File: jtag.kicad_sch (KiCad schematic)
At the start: 5 parts, among them U1 LFE5U-12F-6BG256C

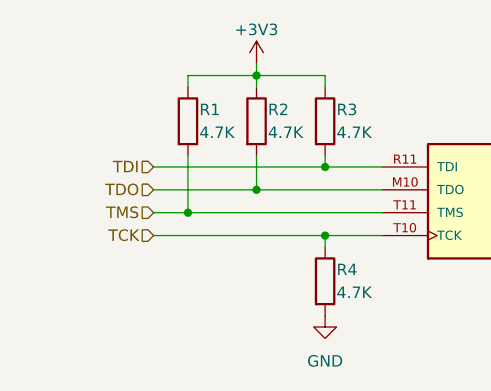
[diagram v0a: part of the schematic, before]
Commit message: Small routing tweaks, add breakout to schematic
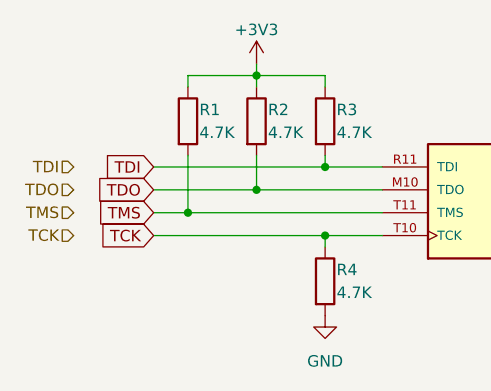
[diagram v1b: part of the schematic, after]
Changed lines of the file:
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@@
     (stroke (width 0) (type default))
   )
-  (hierarchical_label "TMS" (shape input) (at 115.57 44.45 180) (fields_autoplaced)
+  (global_label "TCK" (shape input) (at 115.57 46.99 180) (fields_autoplaced)
+    (effects (font (size 1.27 1.27)) (justify right))
+    (property "Intersheetrefs" "${INTERSHEET_REFS}" (at 109.1566 46.99 0)
+      (effects (font (size 1.27 1.27)) (justify right) hide)
+    )
+  )
+  (global_label "TDO" (shape input) (at 115.57 41.91 180) (fields_autoplaced)
+    (effects (font (size 1.27 1.27)) (justify right))
+    (property "Intersheetrefs" "${INTERSHEET_REFS}" (at 109.0961 41.91 0)
+      (effects (font (size 1.27 1.27)) (justify right) hide)
+    )
+  )
+  (global_label "TMS" (shape input) (at 115.57 44.45 180) (fields_autoplaced)
+    (effects (font (size 1.27 1.27)) (justify right))
+    (property "Intersheetrefs" "${INTERSHEET_REFS}" (at 109.0357 44.45 0)
+      (effects (font (size 1.27 1.27)) (justify right) hide)
+    )
+  )
+  (global_label "TDI" (shape input) (at 115.57 39.37 180) (fields_autoplaced)
+    (effects (font (size 1.27 1.27)) (justify right))
+    (property "Intersheetrefs" "${INTERSHEET_REFS}" (at 109.8218 39.37 0)
+      (effects (font (size 1.27 1.27)) (justify right) hide)
+    )
+  )
+  (hierarchical_label "TDI" (shape input) (at 106.68 39.37 180) (fields_autoplaced)
     (effects (font (size 1.27 1.27)) (justify right))
   )
-  (hierarchical_label "TDO" (shape input) (at 115.57 41.91 180) (fields_autoplaced)
+  (hierarchical_label "TMS" (shape input) (at 106.68 44.45 180) (fields_autoplaced)
     (effects (font (size 1.27 1.27)) (justify right))
   )
-  (hierarchical_label "TDI" (shape input) (at 115.57 39.37 180) (fields_autoplaced)
+  (hierarchical_label "TCK" (shape input) (at 106.68 46.99 180) (fields_autoplaced)
     (effects (font (size 1.27 1.27)) (justify right))
   )
-  (hierarchical_label "TCK" (shape input) (at 115.57 46.99 180) (fields_autoplaced)
+  (hierarchical_label "TDO" (shape input) (at 106.68 41.91 180) (fields_autoplaced)
     (effects (font (size 1.27 1.27)) (justify right))
   )

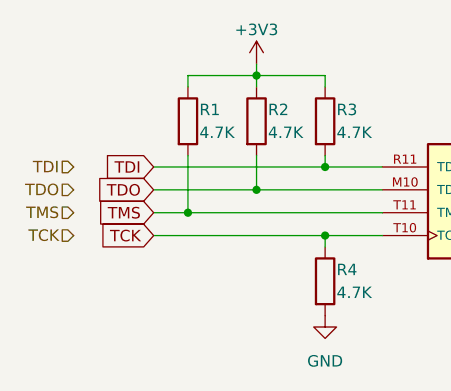
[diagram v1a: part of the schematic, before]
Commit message: Route flash + jtag resistors
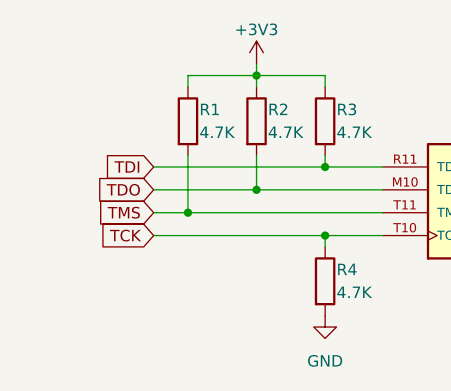
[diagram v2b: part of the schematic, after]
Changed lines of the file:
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@@
     )
-  )
-  (hierarchical_label "TDI" (shape input) (at 106.68 39.37 180) (fields_autoplaced)
-    (effects (font (size 1.27 1.27)) (justify right))
-  )
-  (hierarchical_label "TMS" (shape input) (at 106.68 44.45 180) (fields_autoplaced)
-    (effects (font (size 1.27 1.27)) (justify right))
-  )
-  (hierarchical_label "TCK" (shape input) (at 106.68 46.99 180) (fields_autoplaced)
-    (effects (font (size 1.27 1.27)) (justify right))
-  )
-  (hierarchical_label "TDO" (shape input) (at 106.68 41.91 180) (fields_autoplaced)
-    (effects (font (size 1.27 1.27)) (justify right))
   )
   (symbol (lib_id "Device:R") (at 127 34.29 0) (unit 1)

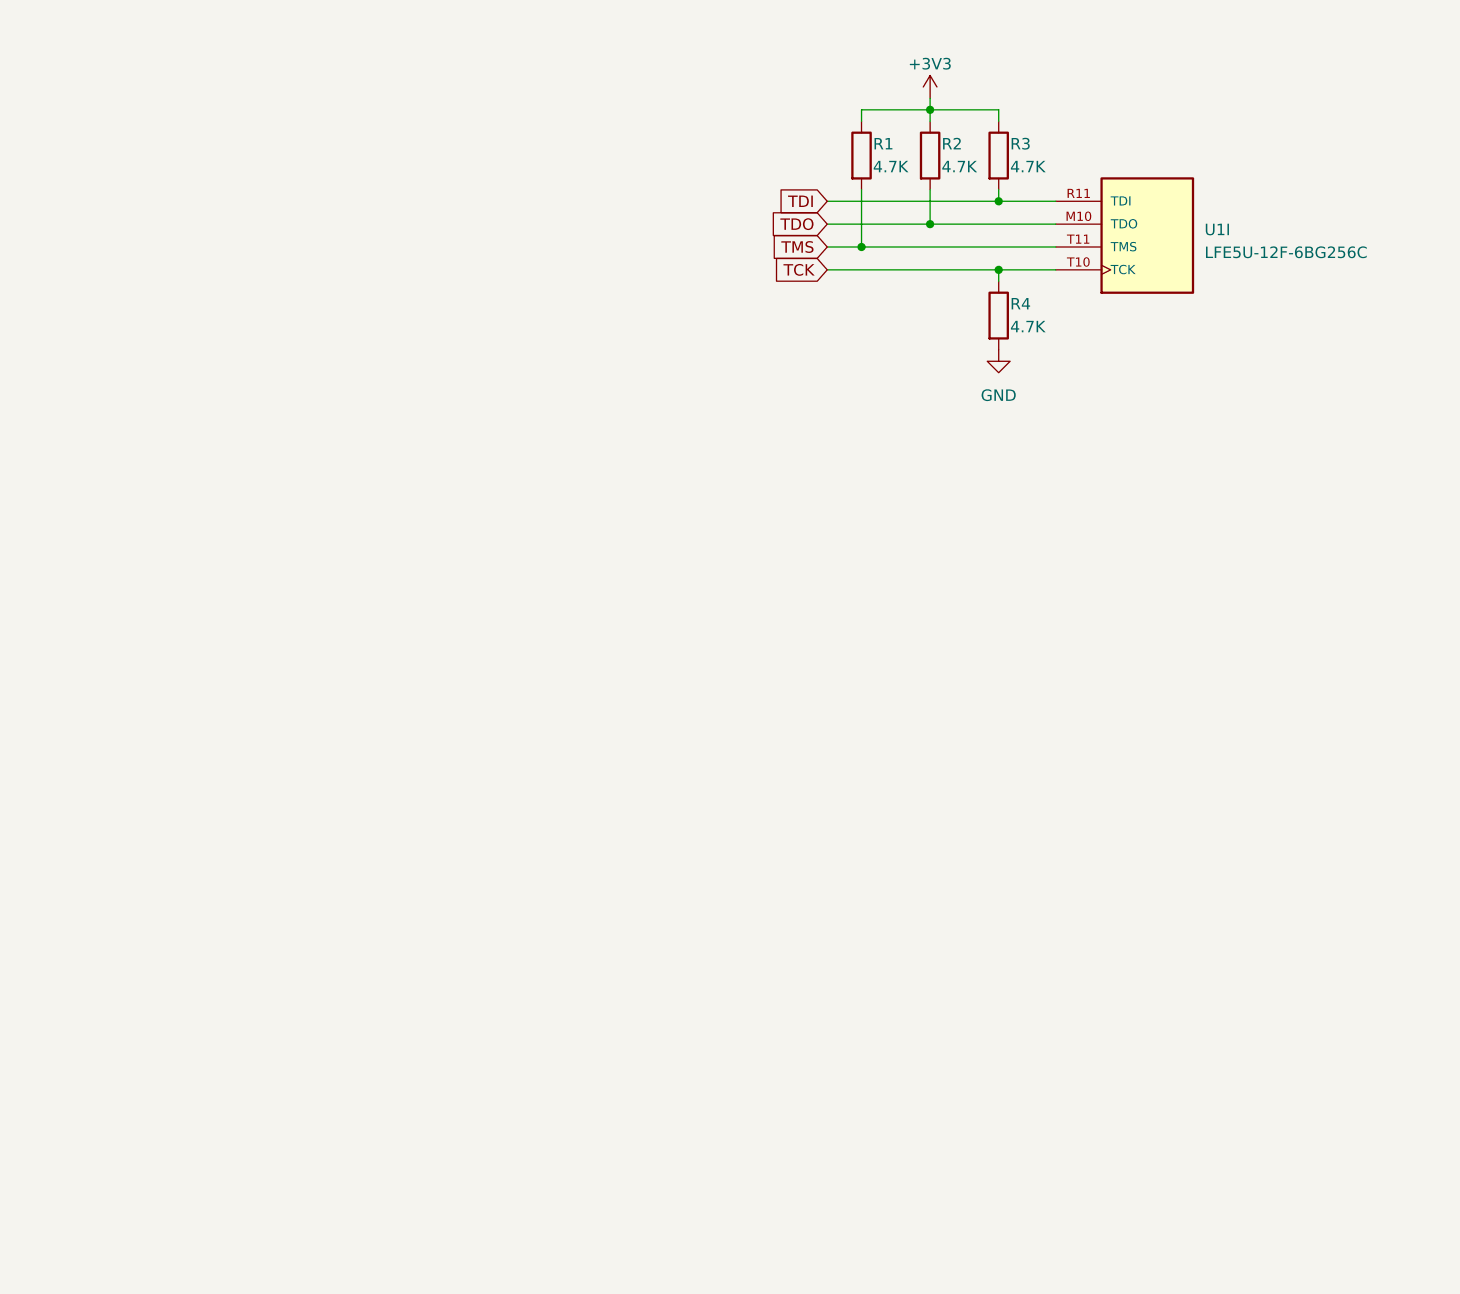
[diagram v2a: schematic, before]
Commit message: Route power, FTDI chip
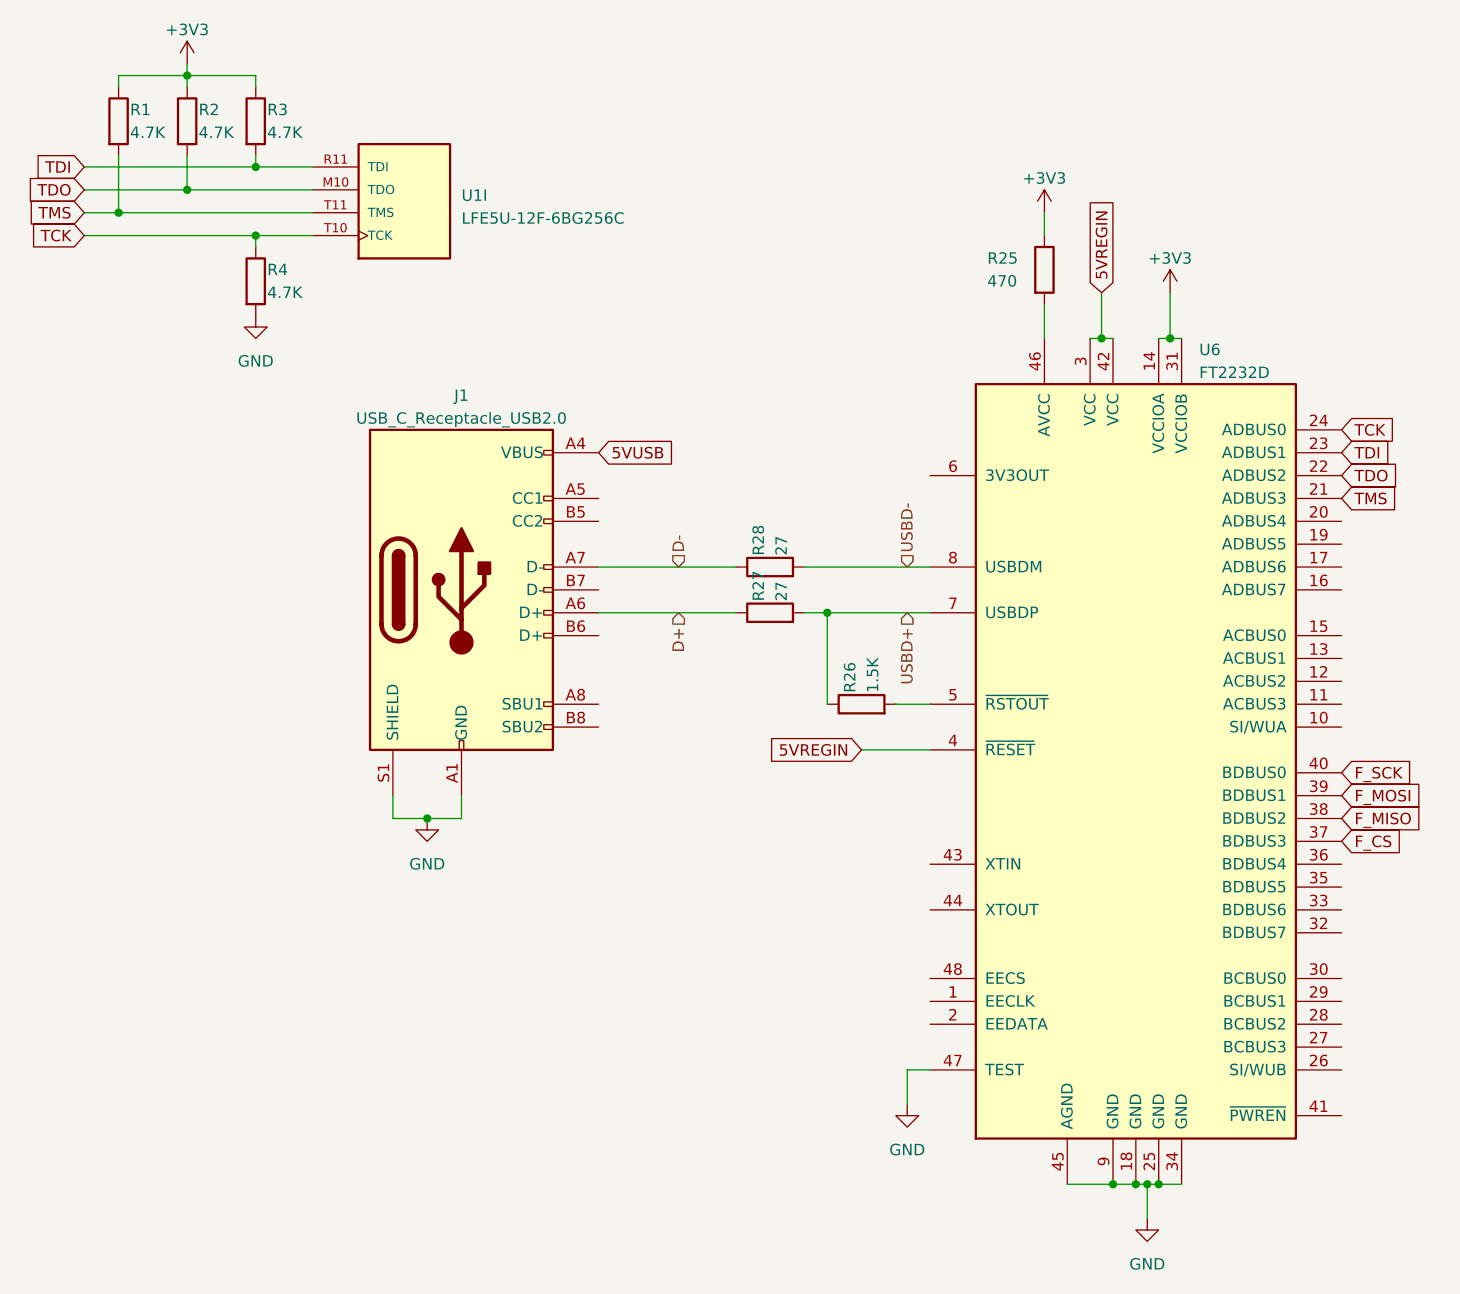
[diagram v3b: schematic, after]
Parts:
- added J1: USB_C_Receptacle_USB2.0, Library:USB_C_GCT4105, symbol Connector:USB_C_Receptacle_USB2.0
- added R25: 470, Resistor_SMD:R_0603_1608Metric, symbol Device:R
- added R26: 1.5K, Resistor_SMD:R_0603_1608Metric, symbol Device:R
- added R27, R28: 27, Resistor_SMD:R_0603_1608Metric, symbol Device:R
- added U6: FT2232D, Package_QFP:LQFP-48_7x7mm_P0.5mm, symbol Interface_USB:FT2232D
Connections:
- net +3V3: now also R25.1, U6.14 (VCCIOA), U6.31 (VCCIOB)
- net GND: now also J1.A1 (GND), J1.A12 (GND), J1.B1 (GND), J1.B12 (GND), J1.S1 (SHIELD), U6.18 (GND), U6.25 (GND), U6.34 (GND), U6.45 (AGND), U6.47 (TEST), U6.9 (GND)
- net TCK: now also U6.24 (ADBUS0)
- net TDI: now also U6.23 (ADBUS1)
- net TDO: now also U6.22 (ADBUS2)
- net TMS: now also U6.21 (ADBUS3)
- new net: R26.2, U6.5 (~{RSTOUT})
- new net: R25.2, U6.46 (AVCC)
- new net 5VREGIN: U6.3 (VCC), U6.4 (~{RESET}), U6.42 (VCC)
- new net 5VUSB: J1.A4 (VBUS), J1.A9 (VBUS), J1.B4 (VBUS), J1.B9 (VBUS)
- new net D+: J1.A6 (D+), R27.1
- new net D-: J1.A7 (D-), R28.1
- new net F_CS: U6.37 (BDBUS3)
- new net F_MISO: U6.38 (BDBUS2)
- new net F_MOSI: U6.39 (BDBUS1)
- new net F_SCK: U6.40 (BDBUS0)
- new net USBD+: R26.1, R27.2, U6.7 (USBDP)
- new net USBD-: R28.2, U6.8 (USBDM)
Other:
- moved on the sheet: R1, R2, R3, R4, U1I
